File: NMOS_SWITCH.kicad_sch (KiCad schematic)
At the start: 22 parts, among them J1 Conn_01x02, J2 Conn_01x02, J3 Conn_01x02, Q1 Q_NPN_BCE, Q2 CSD18540Q5B, U1 BTS443P, U2 LM5050-1

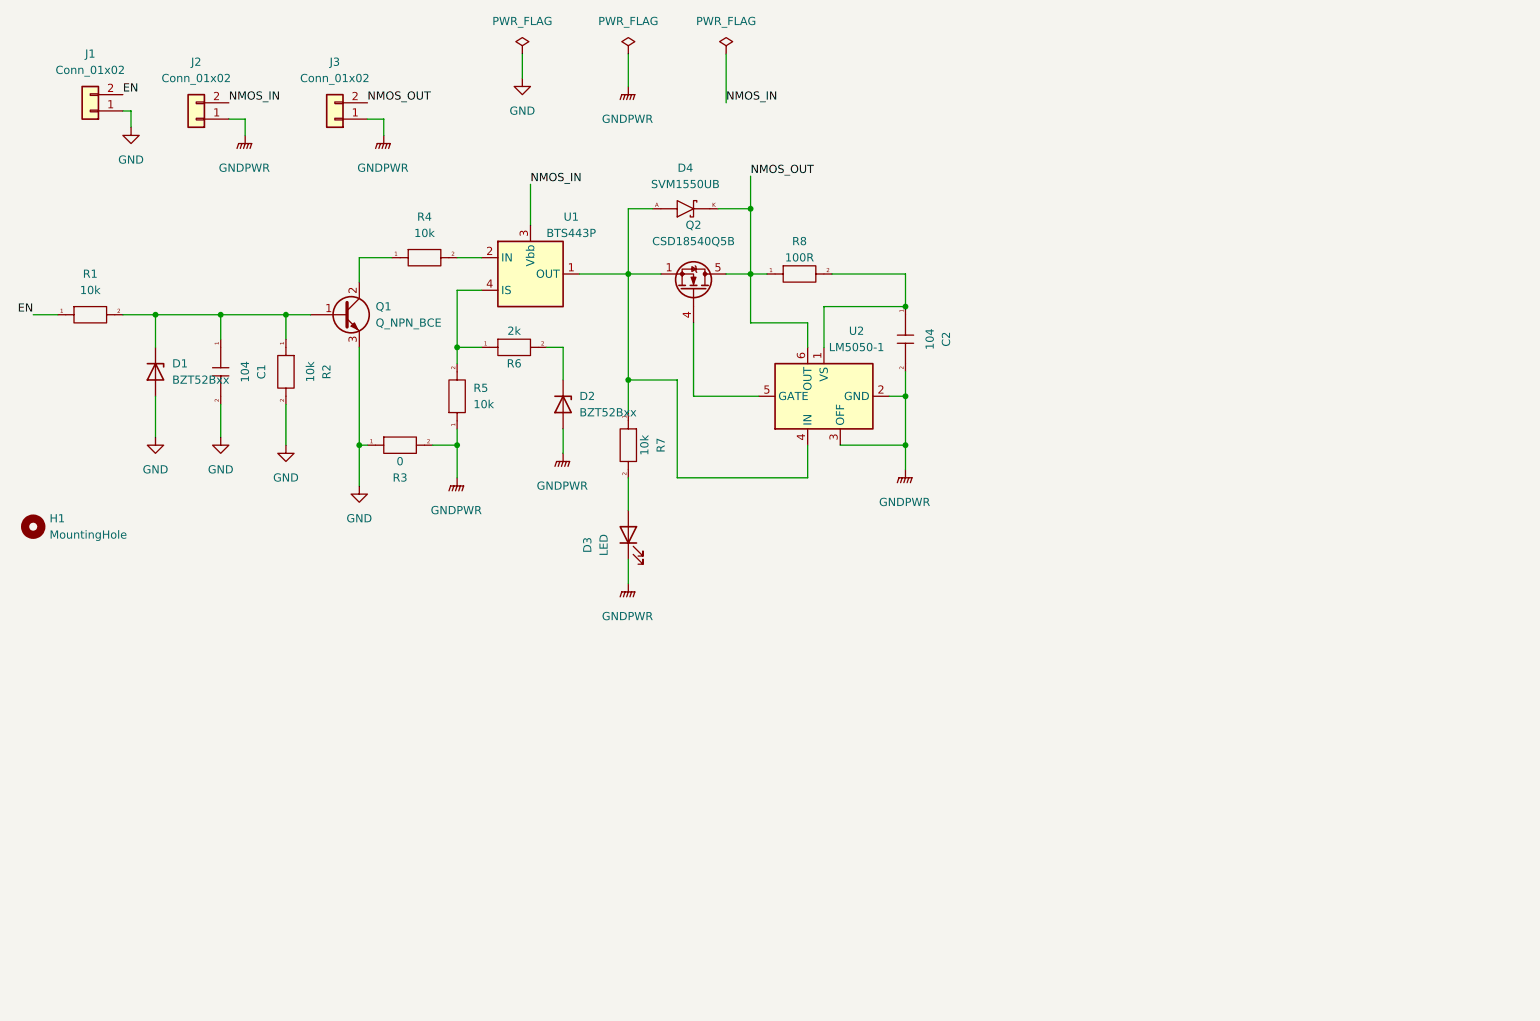
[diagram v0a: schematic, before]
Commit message: Use LM5060, and update PCB
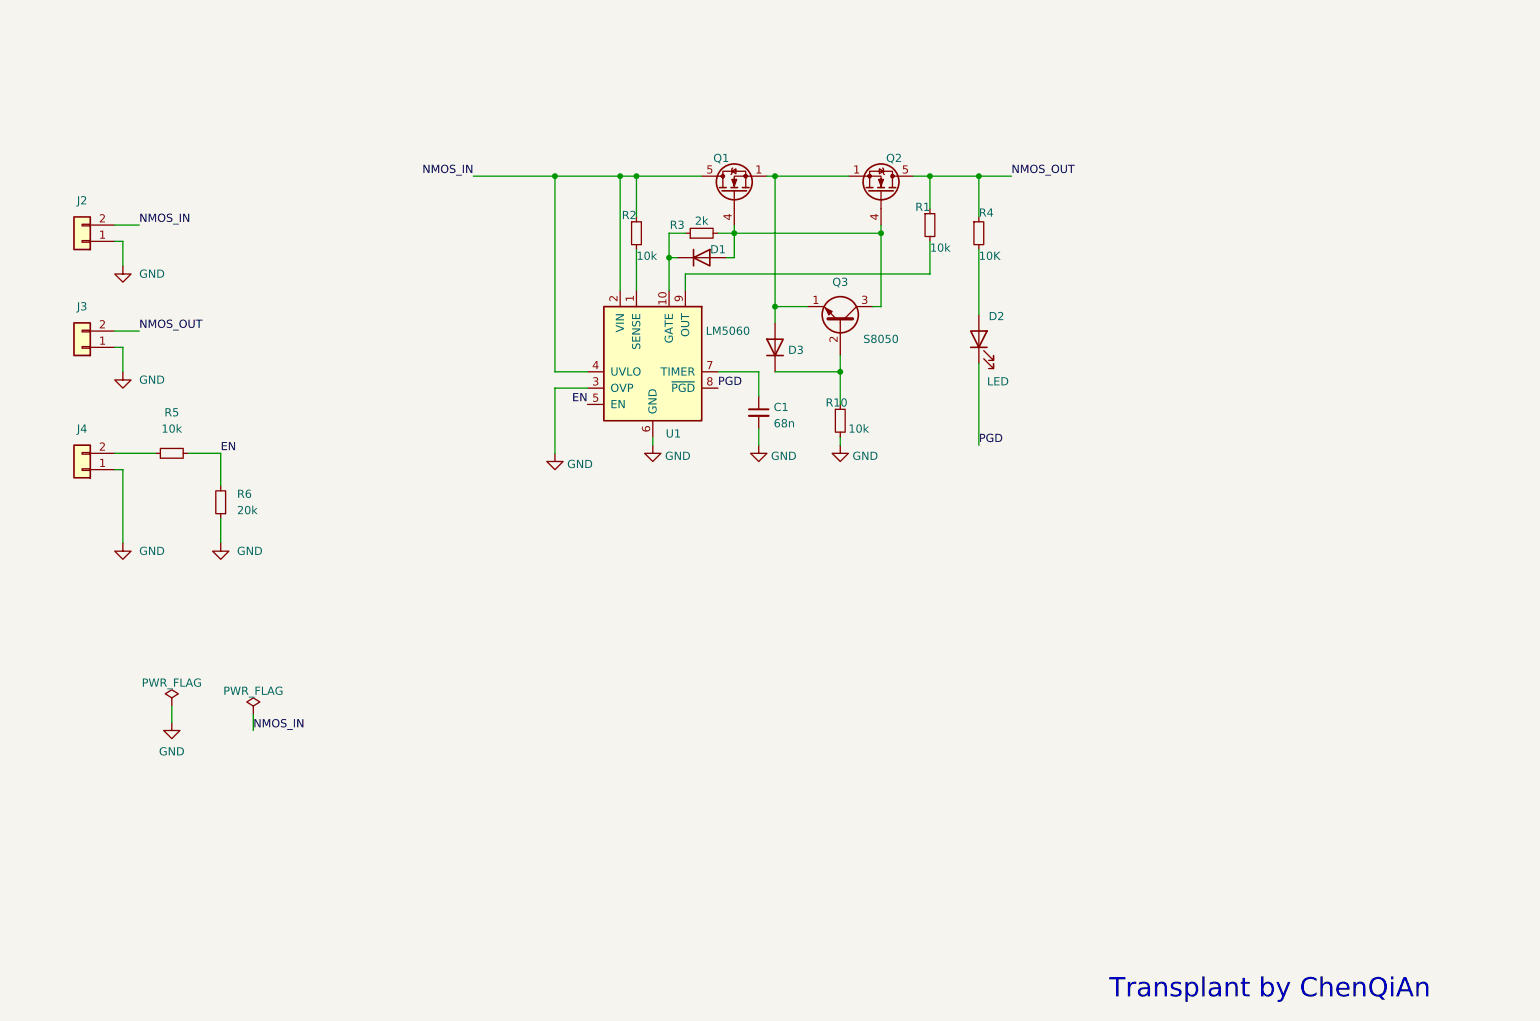
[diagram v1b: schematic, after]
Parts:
- removed C1, C2: 104, Capacitor_SMD:C_0402_1005Metric, symbol Basic_passive_components:Capacitor
- removed D1, D2: BZT52Bxx, Diode_SMD:D_SOD-123F, symbol Diode:BZT52Bxx
- removed D3: LED, LED_SMD:LED_0603_1608Metric, symbol Device:LED
- removed D4: SVM1550UB, POWER_DIODE_SMD:TO-277A, symbol Power_diode:SVM1550UB
- removed H1: MountingHole, MountingHole:MountingHole_3.2mm_M3, symbol Mechanical:MountingHole
- removed J1: Conn_01x02, Connector_AMASS:AMASS_XT30UPB-M_1x02_P5.0mm_Vertical, symbol Connector_Generic:Conn_01x02
- removed Q1: Q_NPN_BCE, Package_TO_SOT_SMD:TSOT-23, symbol Device:Q_NPN_BCE
- removed R1, R2, R4, R5, R7: 10k, Resistor_SMD:R_0402_1005Metric, symbol Basic_passive_components:Resistor
- removed R3: 0, Resistor_SMD:R_0603_1608Metric, symbol Basic_passive_components:Resistor
- removed R6: 2k, Resistor_SMD:R_0402_1005Metric, symbol Basic_passive_components:Resistor
- removed R8: 100R, Resistor_SMD:R_0402_1005Metric, symbol Basic_passive_components:Resistor
- removed U1: BTS443P, Package_TO_SOT_SMD:TO-252-4, symbol Power_Management:BTS443P
- removed U2: LM5050-1, Package_TO_SOT_SMD:TSOT-23-6, symbol Power_Management:LM5050-1
- added C1: 68n, Capacitor_SMD:C_0603_1608Metric, symbol Device:C_Small
- added D1, D3: 1N4001, Diode_SMD:D_SOD-323, symbol Diode:1N4001
- added D2: LED, LED_SMD:LED_0603_1608Metric, symbol Device:LED
- added J4: Conn_01x02, Connector_AMASS:AMASS_XT30PW-M_1x02_P2.50mm_Horizontal, symbol Connector_Generic:Conn_01x02
- added Q1: CSD18540Q5B, Package_TO_SOT_SMD:TDSON-8-1, symbol Transistor_FET:CSD18540Q5B
- added Q3: S8050, Package_TO_SOT_SMD:SOT-23, symbol Transistor_BJT:S8050
- added R1, R10, R2, R5: 10k, Resistor_SMD:R_0603_1608Metric, symbol Device:R_Small
- added R3: 2k, Resistor_SMD:R_0603_1608Metric, symbol Device:R_Small
- added R4: 10K, Resistor_SMD:R_0603_1608Metric, symbol Device:R_Small
- added R6: 20k, Resistor_SMD:R_0603_1608Metric, symbol Device:R_Small
- added U1: LM5060, Package_SO:MSOP-10_3x3mm_P0.5mm, symbol Power_Management:LM5060
- J2: footprint Connector_AMASS:AMASS_XT60-M_1x02_P7.20mm_Vertical -> Connector_AMASS:AMASS_XT30PW-M_1x02_P2.50mm_Horizontal
- J3: footprint Connector_AMASS:AMASS_XT60-F_1x02_P7.20mm_Vertical -> Connector_AMASS:AMASS_XT30PW-F_1x02_P2.50mm_Horizontal
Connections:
- net GNDPWR is gone; now on net GND: J2.1 (Pin_1), J3.1 (Pin_1)
- net EN: now also R5.2, R6.2, U1.5 (EN)
- net GND: now also C1.2, J4.1 (Pin_1), R10.2, R6.1, U1.3 (OVP), U1.6 (GND)
- net NMOS_IN: now also Q1.5 (D), R2.1, U1.2 (VIN), U1.4 (UVLO)
- net NMOS_OUT: now also R1.1, R4.1
- net at Q2.1 (S), Q2.2 (S), Q2.3 (S): now also D3.2 (A), Q1.1 (S), Q1.2 (S), Q1.3 (S), Q3.1 (E)
- net at Q2.4 (G): now also D1.2 (A), Q1.4 (G), Q3.3 (C), R3.2
- new net: R2.2, U1.1 (SENSE)
- new net: D1.1 (K), R3.1, U1.10 (GATE)
- new net: C1.1, U1.7 (TIMER)
- new net: R1.2, U1.9 (OUT)
- new net: J4.2 (Pin_2), R5.1
- new net: D3.1 (K), Q3.2 (B), R10.1
- new net: D2.2 (A), R4.2
- new net PGD: D2.1 (K), U1.8 (~{PGD})
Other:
- note added: "Transplant by ChenQiAn"
